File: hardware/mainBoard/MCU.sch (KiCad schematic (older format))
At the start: 15 parts

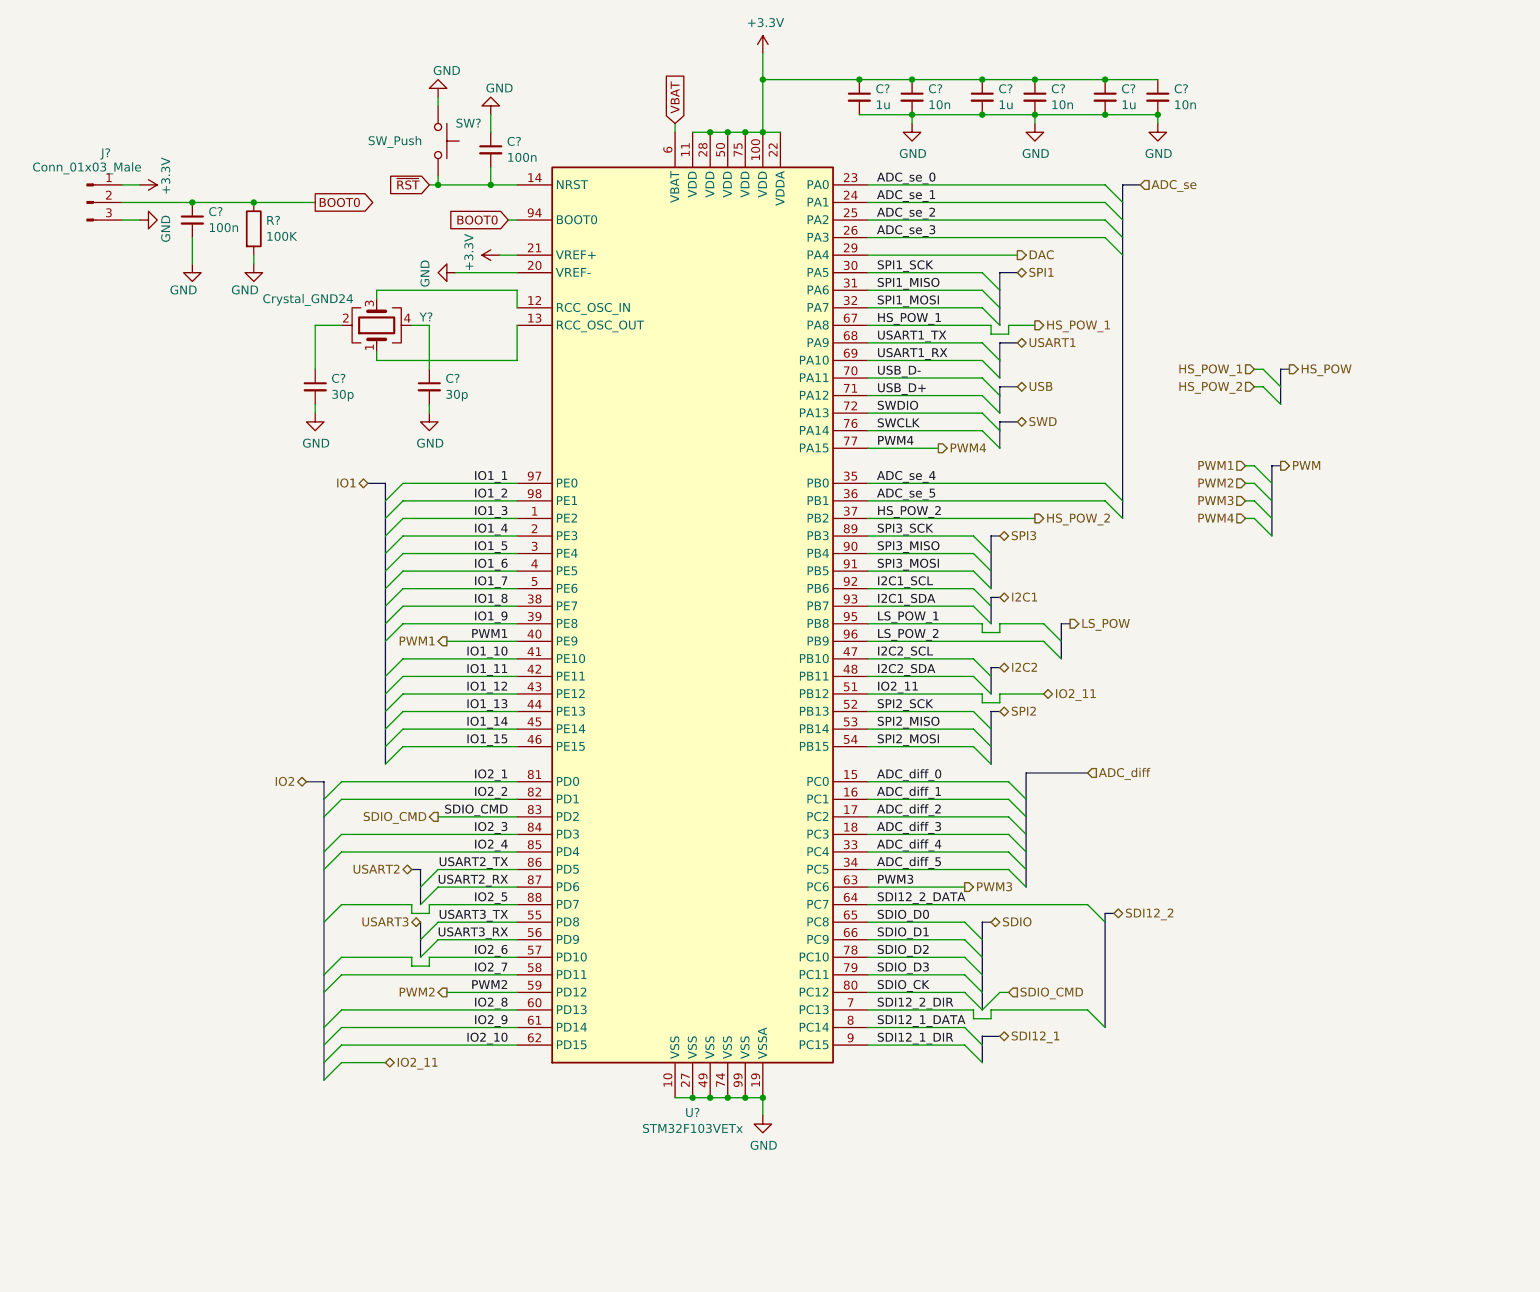
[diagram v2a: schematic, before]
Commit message: Ended schematic, created some pcb footprints
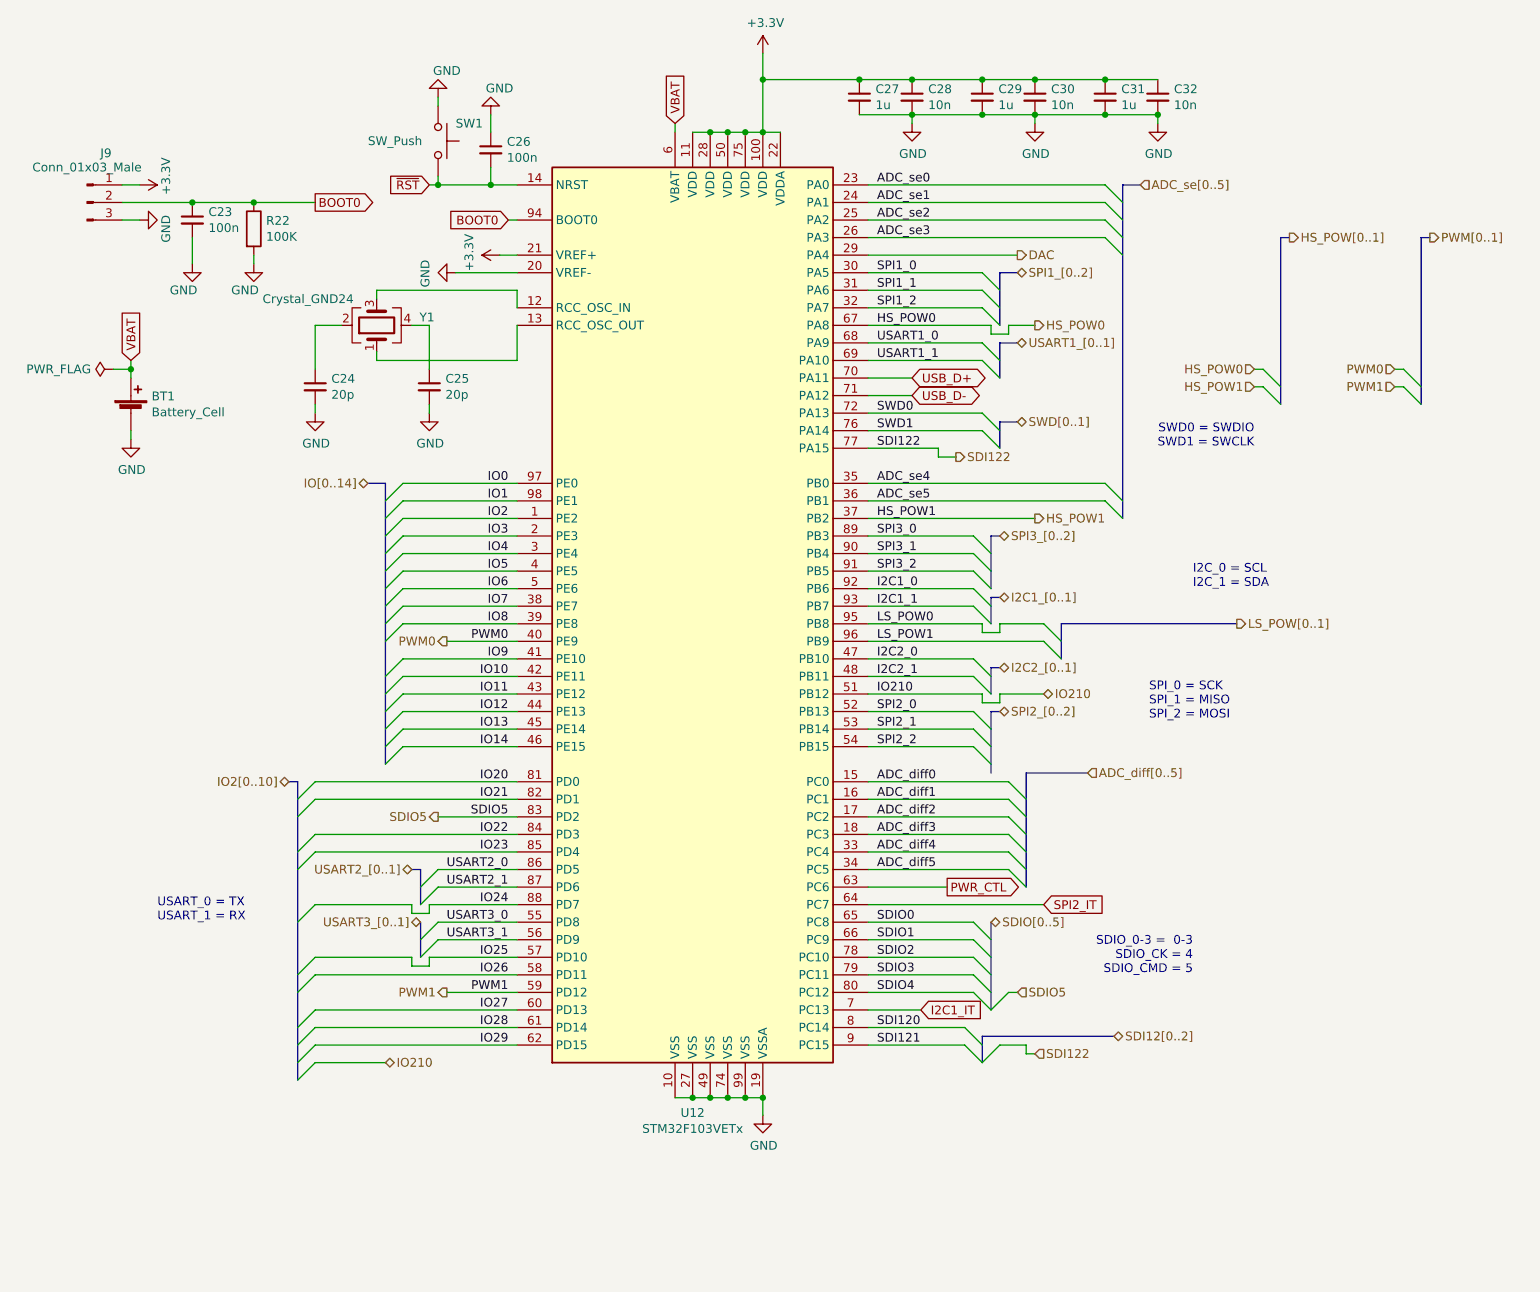
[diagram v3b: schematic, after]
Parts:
- added BT1: Battery_Cell, chinalandfoot:BT-CR2032, symbol Device:Battery_Cell
- C23, C26, C27, C28, C29, C30, C31, C32: renamed from C?; footprint (none) -> Capacitor_SMD:C_0603_1608Metric_Pad1.05x0.95mm_HandSolder
- C24, C25: renamed from C?; value 30p -> 20p; footprint (none) -> Capacitor_SMD:C_0603_1608Metric_Pad1.05x0.95mm_HandSolder
- J9: renamed from J?; footprint (none) -> Connector_PinSocket_2.54mm:PinSocket_1x03_P2.54mm_Vertical
- R22: renamed from R?; footprint (none) -> Resistor_SMD:R_0603_1608Metric_Pad1.05x0.95mm_HandSolder
- SW1: renamed from SW?; footprint (none) -> Button_Switch_THT:SW_PUSH_6mm_H4.3mm
- Y1: renamed from Y?; footprint (none) -> Crystal:Crystal_SMD_7050-4Pin_7.0x5.0mm
- gave numbers to parts that had none: 1
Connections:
- net IO1_2 is gone; now on net IO1: U12.98 (PE1)
- net IO1_3 is gone; now on net IO2: U12.1 (PE2)
- net PWM2 is gone; now on net PWM1: U12.59 (PD12)
- net GND: now also BT1.2 (-)
- net PWM1: no longer U12.40 (PE9)
- net USB_D+: now also U12.70 (PA11); no longer U12.71 (PA12)
- net USB_D-: now also U12.71 (PA12); no longer U12.70 (PA11)
- net VBAT: now also BT1.1 (+)
- net ADC_diff_0 renamed ADC_diff0
- net ADC_diff_1 renamed ADC_diff1
- net ADC_diff_2 renamed ADC_diff2
- net ADC_diff_3 renamed ADC_diff3
- net ADC_diff_4 renamed ADC_diff4
- net ADC_diff_5 renamed ADC_diff5
- net ADC_se_0 renamed ADC_se0
- net ADC_se_1 renamed ADC_se1
- net ADC_se_2 renamed ADC_se2
- net ADC_se_3 renamed ADC_se3
- net ADC_se_4 renamed ADC_se4
- net ADC_se_5 renamed ADC_se5
- net HS_POW_1 renamed HS_POW0
- net HS_POW_2 renamed HS_POW1
- net I2C1_SCL renamed I2C1_0
- net I2C1_SDA renamed I2C1_1
- net I2C2_SCL renamed I2C2_0
- net I2C2_SDA renamed I2C2_1
- net IO1_1 renamed IO0
- net IO1_10 renamed IO9
- net IO1_11 renamed IO10
- net IO1_12 renamed IO11
- net IO1_13 renamed IO12
- net IO1_14 renamed IO13
- net IO1_15 renamed IO14
- net IO1_4 renamed IO3
- net IO1_5 renamed IO4
- net IO1_6 renamed IO5
- net IO1_7 renamed IO6
- net IO1_8 renamed IO7
- net IO1_9 renamed IO8
- net IO2_1 renamed IO20
- net IO2_10 renamed IO29
- net IO2_11 renamed IO210
- net IO2_2 renamed IO21
- net IO2_3 renamed IO22
- net IO2_4 renamed IO23
- net IO2_5 renamed IO24
- net IO2_6 renamed IO25
- net IO2_7 renamed IO26
- net IO2_8 renamed IO27
- net IO2_9 renamed IO28
- net LS_POW_1 renamed LS_POW0
- net LS_POW_2 renamed LS_POW1
- net PWM3 renamed PWR_CTL
- net PWM4 renamed SDI122
- net SDI12_1_DATA renamed SDI120
- net SDI12_1_DIR renamed SDI121
- net SDI12_2_DATA renamed SPI2_IT
- net SDI12_2_DIR renamed I2C1_IT
- net SDIO_CK renamed SDIO4
- net SDIO_CMD renamed SDIO5
- net SDIO_D0 renamed SDIO0
- net SDIO_D1 renamed SDIO1
- net SDIO_D2 renamed SDIO2
- net SDIO_D3 renamed SDIO3
- net SPI1_MISO renamed SPI1_1
- net SPI1_MOSI renamed SPI1_2
- net SPI1_SCK renamed SPI1_0
- net SPI2_MISO renamed SPI2_1
- net SPI2_MOSI renamed SPI2_2
- net SPI2_SCK renamed SPI2_0
- net SPI3_MISO renamed SPI3_1
- net SPI3_MOSI renamed SPI3_2
- net SPI3_SCK renamed SPI3_0
- net SWCLK renamed SWD1
- net SWDIO renamed SWD0
- net USART1_RX renamed USART1_1
- net USART1_TX renamed USART1_0
- net USART2_RX renamed USART2_1
- net USART2_TX renamed USART2_0
- net USART3_RX renamed USART3_1
- net USART3_TX renamed USART3_0
- new net PWM0: U12.40 (PE9)
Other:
- note added: "I2C_0 = SCL\nI2C_1 = SDA"
- note added: "SDIO_0-3 = 0-3\nSDIO_CK = 4\nSDIO_CMD = 5"
- note added: "SPI_0 = SCK\nSPI_1 = MISO\nSPI_2 = MOSI"
- note added: "SWD0 = SWDIO\nSWD1 = SWCLK"
- note added: "USART_0 = TX\nUSART_1 = RX"

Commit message: PCB finished
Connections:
- net GND: now also Y1.2, Y1.4
- net at U12.12 (RCC_OSC_IN), Y1.3: now also C24.1
- net at U12.13 (RCC_OSC_OUT), Y1.1: now also C25.1
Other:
- moved on the sheet: C24, C25
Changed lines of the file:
@@
 EESchema Schematic File Version 4
-LIBS:prockeckv2-cache
 EELAYER 30 0
 EELAYER END
@@
 Wire Wire Line
 	3300 2200 3300 2100
-Wire Wire Line
-	3300 2100 2500 2100
-Wire Wire Line
-	2500 2100 2500 2150
-$Comp
-L Device:C_Small C24
-U 1 1 5DD6A3FD
-P 2150 2650
-F 0 "C24" H 2242 2696 50  0000 L CNN
-F 1 "20p" H 2242 2605 50  0000 L CNN
-F 2 "Capacitor_SMD:C_0603_1608Metric_Pad1.05x0.95mm_HandSolder" H 2150 2650 50  0001 C CNN
-F 3 "~" H 2150 2650 50  0001 C CNN
-	1    2150 2650
-	1    0    0    -1
-$EndComp
 $Comp
 L Device:C_Small C25
 U 1 1 5DD6AE7A
-P 2800 2650
-F 0 "C25" H 2892 2696 50  0000 L CNN
-F 1 "20p" H 2892 2605 50  0000 L CNN
-F 2 "Capacitor_SMD:C_0603_1608Metric_Pad1.05x0.95mm_HandSolder" H 2800 2650 50  0001 C CNN
-F 3 "~" H 2800 2650 50  0001 C CNN
-	1    2800 2650
-	1    0    0    -1
-$EndComp
-Wire Wire Line
-	2300 2300 2150 2300
-Wire Wire Line
-	2150 2300 2150 2550
+P 2500 2650
+F 0 "C25" H 2592 2696 50  0000 L CNN
+F 1 "20p" H 2592 2605 50  0000 L CNN
+F 2 "Capacitor_SMD:C_0603_1608Metric_Pad1.05x0.95mm_HandSolder" H 2500 2650 50  0001 C CNN
+F 3 "~" H 2500 2650 50  0001 C CNN
+	1    2500 2650
+	1    0    0    -1
+$EndComp
 $Comp
 L Device:Crystal_GND24 Y1
 U 1 1 5DD5F9B1
 P 2500 2300
-F 0 "Y1" V 2546 2056 50  0000 R CNN
+F 0 "Y1" V 2600 2100 50  0000 R CNN
 F 1 "Crystal_GND24" V 2650 2950 50  0000 R CNN
 F 2 "Crystal:Crystal_SMD_7050-4Pin_7.0x5.0mm" H 2500 2300 50  0001 C CNN
@@
 $EndComp
 Wire Wire Line
-	2800 2550 2800 2300
-Wire Wire Line
-	2800 2300 2700 2300
+	2750 2300 2700 2300
 $Comp
 L power:GND #PWR058
 U 1 1 5DD72FF6
-P 2800 2800
-F 0 "#PWR058" H 2800 2550 50  0001 C CNN
-F 1 "GND" H 2805 2627 50  0000 C CNN
-F 2 "" H 2800 2800 50  0001 C CNN
-F 3 "" H 2800 2800 50  0001 C CNN
-	1    2800 2800
-	1    0    0    -1
-$EndComp
-Wire Wire Line
-	2800 2800 2800 2750
+P 2500 2800
+F 0 "#PWR058" H 2500 2550 50  0001 C CNN
+F 1 "GND" H 2505 2627 50  0000 C CNN
+F 2 "" H 2500 2800 50  0001 C CNN
+F 3 "" H 2500 2800 50  0001 C CNN
+	1    2500 2800
+	1    0    0    -1
+$EndComp
+Wire Wire Line
+	2500 2800 2500 2750
 $Comp
 L power:GND #PWR057
 U 1 1 5DD74202
-P 2150 2800
-F 0 "#PWR057" H 2150 2550 50  0001 C CNN
-F 1 "GND" H 2155 2627 50  0000 C CNN
-F 2 "" H 2150 2800 50  0001 C CNN
-F 3 "" H 2150 2800 50  0001 C CNN
-	1    2150 2800
-	1    0    0    -1
-$EndComp
-Wire Wire Line
-	2150 2800 2150 2750
+P 2500 1800
+F 0 "#PWR057" H 2500 1550 50  0001 C CNN
+F 1 "GND" H 2505 1627 50  0000 C CNN
+F 2 "" H 2500 1800 50  0001 C CNN
+F 3 "" H 2500 1800 50  0001 C CNN
+	1    2500 1800
+	-1   0    0    1
+$EndComp
 Wire Wire Line
 	5300 4900 6100 4900
@@
 	1    0    0    -1
 $EndComp
-Text GLabel 2150 1600 2    50   Output ~ 0
+Text GLabel 2050 1600 2    50   Output ~ 0
 BOOT0
 Wire Wire Line
-	2150 1600 1800 1600
+	2050 1600 1800 1600
 $Comp
 L power:GND #PWR054
@@
 Wire Wire Line
 	1100 2550 1100 2600
+Wire Wire Line
+	2500 1800 2500 1850
+Wire Wire Line
+	2500 2100 2500 2150
+Wire Wire Line
+	3300 2100 2500 2100
+$Comp
+L Device:C_Small C24
+U 1 1 5DD6A3FD
+P 2500 1950
+F 0 "C24" H 2592 1996 50  0000 L CNN
+F 1 "20p" H 2592 1905 50  0000 L CNN
+F 2 "Capacitor_SMD:C_0603_1608Metric_Pad1.05x0.95mm_HandSolder" H 2500 1950 50  0001 C CNN
+F 3 "~" H 2500 1950 50  0001 C CNN
+	1    2500 1950
+	-1   0    0    1
+$EndComp
+Wire Wire Line
+	2500 2050 2500 2100
+Connection ~ 2500 2100
+Wire Wire Line
+	2500 2550 2500 2500
+Connection ~ 2500 2500
+$Comp
+L power:GND #PWR?
+U 1 1 5E168D3A
+P 2250 2300
+F 0 "#PWR?" H 2250 2050 50  0001 C CNN
+F 1 "GND" H 2255 2127 50  0000 C CNN
+F 2 "" H 2250 2300 50  0001 C CNN
+F 3 "" H 2250 2300 50  0001 C CNN
+	1    2250 2300
+	0    1    1    0
+$EndComp
+Wire Wire Line
+	2250 2300 2300 2300
+$Comp
+L power:GND #PWR?
+U 1 1 5E1765D4
+P 2750 2300
+F 0 "#PWR?" H 2750 2050 50  0001 C CNN
+F 1 "GND" H 2755 2127 50  0000 C CNN
+F 2 "" H 2750 2300 50  0001 C CNN
+F 3 "" H 2750 2300 50  0001 C CNN
+	1    2750 2300
+	0    -1   -1   0
+$EndComp
 Wire Bus Line
 	8450 1800 8450 2750

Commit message: First working software
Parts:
- BT1: URL (none) -> https://lcsc.com/product-detail/Battery-Holders-Clips-Conta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
- C23, C24, C25, C26, C27, C28, C29, C30, C31, C32: URL (none) -> https://lcsc.com/product-detail/Multilayer-Ceramic-Capacito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
- R22: value 100K -> 100k; URL (none) -> https://lcsc.com/product-detail/Chip-Resistor-Surface-Mount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
- SW1: URL (none) -> https://lcsc.com/product-detail/Tactile-Switches_Korean-Hro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
- U12: URL (none) -> https://lcsc.com/product-detail/ST-Microelectronics_STMicro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
- Y1: URL (none) -> https://lcsc.com/product-detail/SMD-Crystal-Resonators_Yang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
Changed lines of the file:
@@
 EESchema Schematic File Version 4
+LIBS:prockeckv2-cache
 EELAYER 30 0
 EELAYER END
@@
 F 2 "Capacitor_SMD:C_0603_1608Metric_Pad1.05x0.95mm_HandSolder" H 5950 1000 50  0001 C CNN
 F 3 "~" H 5950 1000 50  0001 C CNN
+F 4 "https://lcsc.com/product-detail/Multilayer-Ceramic-Capacitors-MLCC-SMD-SMT_SAMSUNG_CL10A105KB8NNNC_1uF-105-10-50V_C15849.html" H 5950 1000 50  0001 C CNN "URL"
 	1    5950 1000
 	1    0    0    -1
@@
 F 2 "Package_QFP:LQFP-100_14x14mm_P0.5mm" H 3500 1300 50  0001 R CNN
 F 3 "http://www.st.com/st-web-ui/static/active/en/resource/technical/document/datasheet/CD00191185.pdf" H 4300 3900 50  0001 C CNN
+F 4 "https://lcsc.com/product-detail/ST-Microelectronics_STMicroelectronics_STM32F103VET6_STM32F103VET6_C8308.html" H 4300 3900 50  0001 C CNN "URL"
 	1    4300 3900
 	1    0    0    -1
@@
 F 2 "Capacitor_SMD:C_0603_1608Metric_Pad1.05x0.95mm_HandSolder" H 6250 1000 50  0001 C CNN
 F 3 "~" H 6250 1000 50  0001 C CNN
+F 4 "https://lcsc.com/product-detail/Multilayer-Ceramic-Capacitors-MLCC-SMD-SMT_FH-Guangdong-Fenghua-Advanced-Tech-0603B103K500NT_C57112.html" H 6250 1000 50  0001 C CNN "URL"
 	1    6250 1000
 	1    0    0    -1
@@
 F 2 "Capacitor_SMD:C_0603_1608Metric_Pad1.05x0.95mm_HandSolder" H 5250 1000 50  0001 C CNN
 F 3 "~" H 5250 1000 50  0001 C CNN
+F 4 "https://lcsc.com/product-detail/Multilayer-Ceramic-Capacitors-MLCC-SMD-SMT_SAMSUNG_CL10A105KB8NNNC_1uF-105-10-50V_C15849.html" H 5250 1000 50  0001 C CNN "URL"
 	1    5250 1000
 	1    0    0    -1
@@
 F 2 "Capacitor_SMD:C_0603_1608Metric_Pad1.05x0.95mm_HandSolder" H 5550 1000 50  0001 C CNN
 F 3 "~" H 5550 1000 50  0001 C CNN
+F 4 "https://lcsc.com/product-detail/Multilayer-Ceramic-Capacitors-MLCC-SMD-SMT_FH-Guangdong-Fenghua-Advanced-Tech-0603B103K500NT_C57112.html" H 5550 1000 50  0001 C CNN "URL"
 	1    5550 1000
 	1    0    0    -1
@@
 F 2 "Capacitor_SMD:C_0603_1608Metric_Pad1.05x0.95mm_HandSolder" H 6650 1000 50  0001 C CNN
 F 3 "~" H 6650 1000 50  0001 C CNN
+F 4 "https://lcsc.com/product-detail/Multilayer-Ceramic-Capacitors-MLCC-SMD-SMT_SAMSUNG_CL10A105KB8NNNC_1uF-105-10-50V_C15849.html" H 6650 1000 50  0001 C CNN "URL"
 	1    6650 1000
 	1    0    0    -1
@@
 F 2 "Capacitor_SMD:C_0603_1608Metric_Pad1.05x0.95mm_HandSolder" H 6950 1000 50  0001 C CNN
 F 3 "~" H 6950 1000 50  0001 C CNN
+F 4 "https://lcsc.com/product-detail/Multilayer-Ceramic-Capacitors-MLCC-SMD-SMT_FH-Guangdong-Fenghua-Advanced-Tech-0603B103K500NT_C57112.html" H 6950 1000 50  0001 C CNN "URL"
 	1    6950 1000
 	1    0    0    -1
@@
 F 2 "Capacitor_SMD:C_0603_1608Metric_Pad1.05x0.95mm_HandSolder" H 2500 2650 50  0001 C CNN
 F 3 "~" H 2500 2650 50  0001 C CNN
+F 4 "https://lcsc.com/product-detail/Multilayer-Ceramic-Capacitors-MLCC-SMD-SMT_SAMSUNG_CL10C200JB8NNNC_20pF-200-5-50V_C1648.html" H 2500 2650 50  0001 C CNN "URL"
 	1    2500 2650
 	1    0    0    -1
@@
 F 5 "Yangxing Tech X50328MSB4SI" V 2500 2300 50  0001 C CNN "Nombre"
 F 6 "https://www.st.com/content/ccc/resource/technical/document/application_note/c6/eb/5e/11/e3/69/43/eb/CD00221665.pdf/files/CD00221665.pdf/jcr:content/translations/en.CD00221665.pdf" V 2500 2300 50  0001 C CNN "Calculo2"
+F 7 "https://lcsc.com/product-detail/SMD-Crystal-Resonators_Yangxing-Tech-X50328MSB4SI_C157341.html" H 2500 2300 50  0001 C CNN "URL"
 	1    2500 2300
 	0    -1   -1   0
@@
 P 1800 1750
 F 0 "R22" H 1870 1796 50  0000 L CNN
-F 1 "100K" H 1870 1705 50  0000 L CNN
+F 1 "100k" H 1870 1705 50  0000 L CNN
 F 2 "Resistor_SMD:R_0603_1608Metric_Pad1.05x0.95mm_HandSolder" V 1730 1750 50  0001 C CNN
 F 3 "~" H 1800 1750 50  0001 C CNN
+F 4 "https://lcsc.com/product-detail/Chip-Resistor-Surface-Mount_100KR-1003-1_C14675.html" H 1800 1750 50  0001 C CNN "URL"
 	1    1800 1750
 	1    0    0    -1
@@
 F 2 "Capacitor_SMD:C_0603_1608Metric_Pad1.05x0.95mm_HandSolder" H 1450 1700 50  0001 C CNN
 F 3 "~" H 1450 1700 50  0001 C CNN
+F 4 "https://lcsc.com/product-detail/Multilayer-Ceramic-Capacitors-MLCC-SMD-SMT_SAMSUNG_CL10F104ZB8NNNC_100nF-104-80-20-50V_C1688.html" H 1450 1700 50  0001 C CNN "URL"
 	1    1450 1700
 	1    0    0    -1
@@
 F 2 "Capacitor_SMD:C_0603_1608Metric_Pad1.05x0.95mm_HandSolder" H 3150 1300 50  0001 C CNN
 F 3 "~" H 3150 1300 50  0001 C CNN
+F 4 "https://lcsc.com/product-detail/Multilayer-Ceramic-Capacitors-MLCC-SMD-SMT_SAMSUNG_CL10F104ZB8NNNC_100nF-104-80-20-50V_C1688.html" H 3150 1300 50  0001 C CNN "URL"
 	1    3150 1300
 	1    0    0    -1
@@
 F 2 "Button_Switch_THT:SW_PUSH_6mm_H4.3mm" H 2850 1450 50  0001 C CNN
 F 3 "~" H 2850 1450 50  0001 C CNN
+F 4 "https://lcsc.com/product-detail/Tactile-Switches_Korean-Hroparts-Elec-K2-1102DP-C4SW-04_C110153.html" H 2850 1250 50  0001 C CNN "URL"
 	1    2850 1250
 	0    1    1    0
@@
 F 2 "chinalandfoot:BT-CR2032" V 1100 2860 50  0001 C CNN
 F 3 "~" V 1100 2860 50  0001 C CNN
+F 4 "https://lcsc.com/product-detail/Battery-Holders-Clips-Contacts_Button-battery-holder-CR2032_C70377.html" H 1100 2800 50  0001 C CNN "URL"
 	1    1100 2800
 	1    0    0    -1
@@
 F 2 "Capacitor_SMD:C_0603_1608Metric_Pad1.05x0.95mm_HandSolder" H 2500 1950 50  0001 C CNN
 F 3 "~" H 2500 1950 50  0001 C CNN
+F 4 "https://lcsc.com/product-detail/Multilayer-Ceramic-Capacitors-MLCC-SMD-SMT_SAMSUNG_CL10C200JB8NNNC_20pF-200-5-50V_C1648.html" H 2500 1950 50  0001 C CNN "URL"
 	1    2500 1950
 	-1   0    0    1
@@
 Connection ~ 2500 2500
 $Comp
-L power:GND #PWR?
+L power:GND #PWR0130
 U 1 1 5E168D3A
 P 2250 2300
-F 0 "#PWR?" H 2250 2050 50  0001 C CNN
+F 0 "#PWR0130" H 2250 2050 50  0001 C CNN
 F 1 "GND" H 2255 2127 50  0000 C CNN
 F 2 "" H 2250 2300 50  0001 C CNN
@@
 	2250 2300 2300 2300
 $Comp
-L power:GND #PWR?
+L power:GND #PWR0131
 U 1 1 5E1765D4
 P 2750 2300
-F 0 "#PWR?" H 2750 2050 50  0001 C CNN
+F 0 "#PWR0131" H 2750 2050 50  0001 C CNN
 F 1 "GND" H 2755 2127 50  0000 C CNN
 F 2 "" H 2750 2300 50  0001 C CNN
